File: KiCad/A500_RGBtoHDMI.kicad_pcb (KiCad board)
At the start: 2 copper layers, 80 x 29.5 mm, 19 parts, among them J1 Conn_02x20_Odd_Even, J2 Conn_01x02, U1 Denise_Socket, U2 XC9572XL-VQ64, U3 LM1117-3.3, U4 Denise_MB_PinHeader

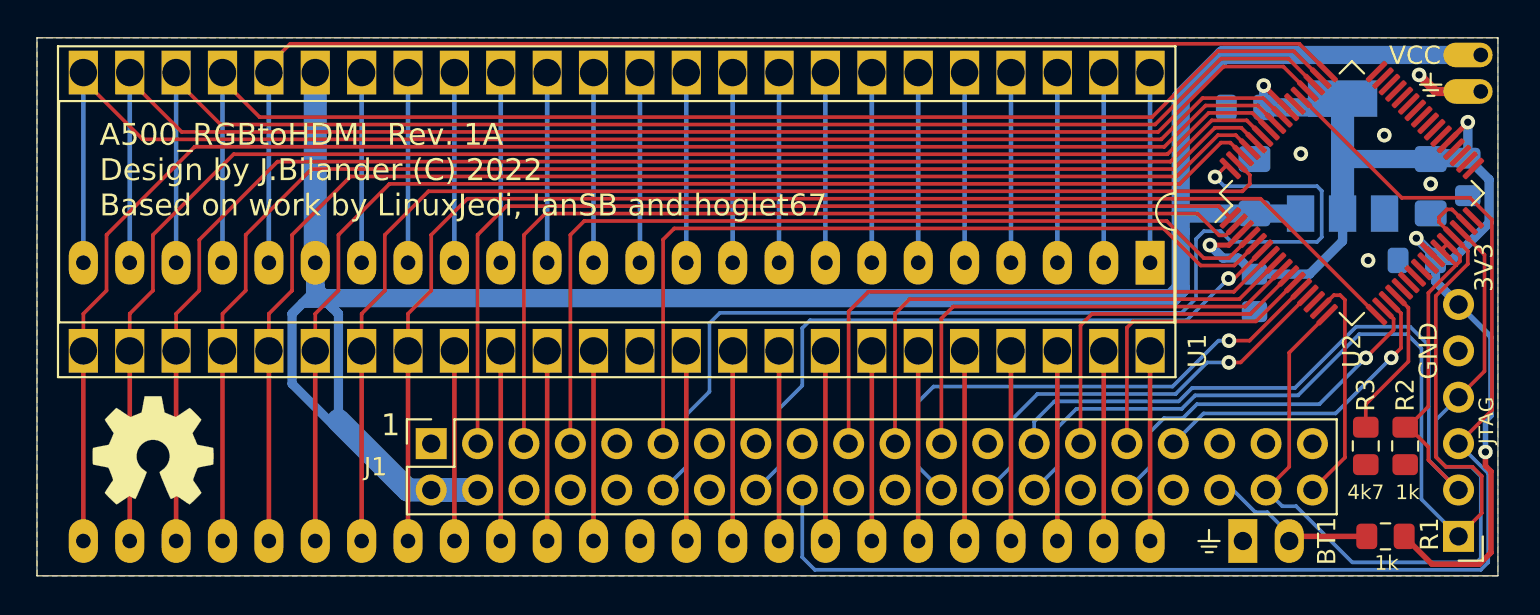
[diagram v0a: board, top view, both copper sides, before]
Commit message: add CSYNC-PinHeader for Rev3 A500-mobos
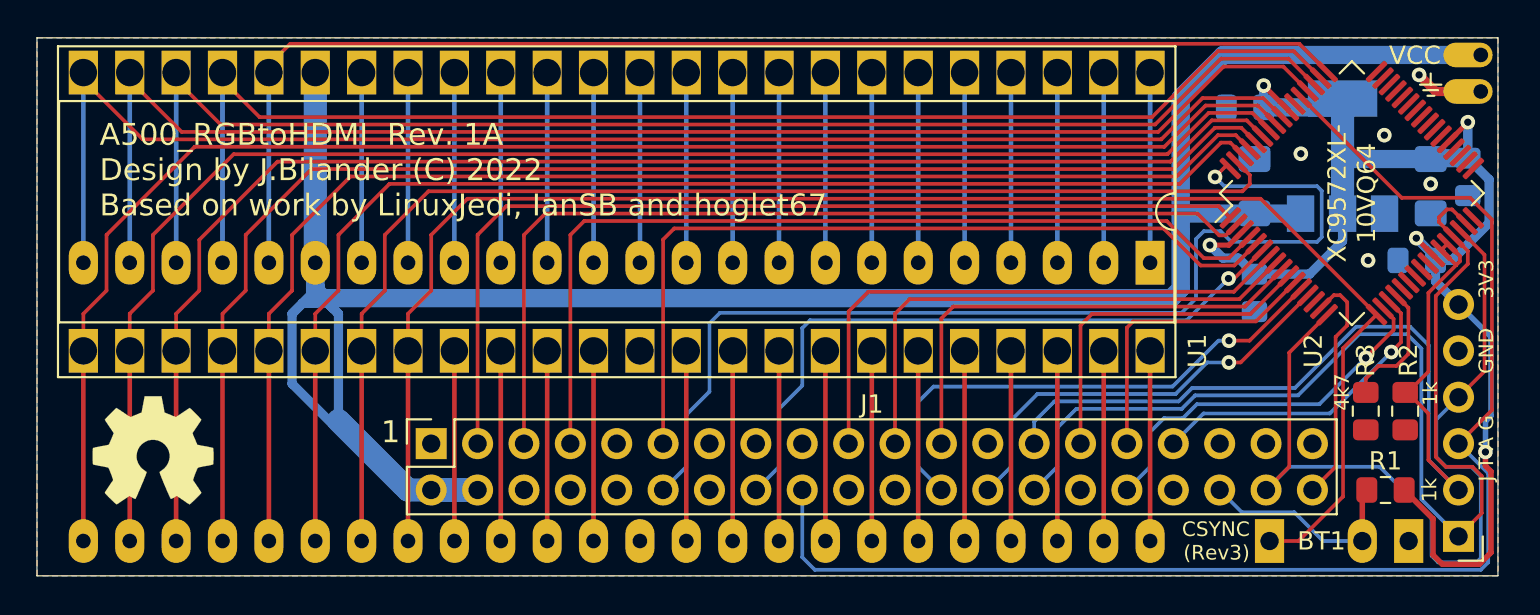
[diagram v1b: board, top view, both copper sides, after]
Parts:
- added J3: Conn_01x01, Connector_PinHeader_2.54mm:PinHeader_1x01_P2.54mm_Horizontal, F.Cu at (194.5, 103.4)
- BT1: moved to F.Cu
- moved BT1 9.08 mm to (202.1, 103.4)
- moved R1 2.54 mm to (200.9, 100.6)
- moved R2 1.91 mm to (201.9, 96.3)
- moved R3 1.91 mm to (199.8, 96.3)
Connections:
- net Net-(U2-Pad48) renamed VSYNC
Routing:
- net CSYNC: track 72.5 -> 88.4 mm
- net TCK_SPCLK: track 45.9 -> 48.1 mm
- net 3V3: track 70.8 -> 73.0 mm
- net Net-(BT1-Pad2): track 9.54 -> 11.7 mm
- net DETECT: track 8.48 -> 7.14 mm
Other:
- net class Default: clearance 0.2032 -> 0.1524
- rule trace_clearance: 0.2032 -> 0.1524
- board text added: "CSYNC"
- board text added: "CSYNC (Rev3)"
- board text added: "J T A G"
- board text added: "XC9572XL- 10VQ64"
- board text removed: "JTAG"

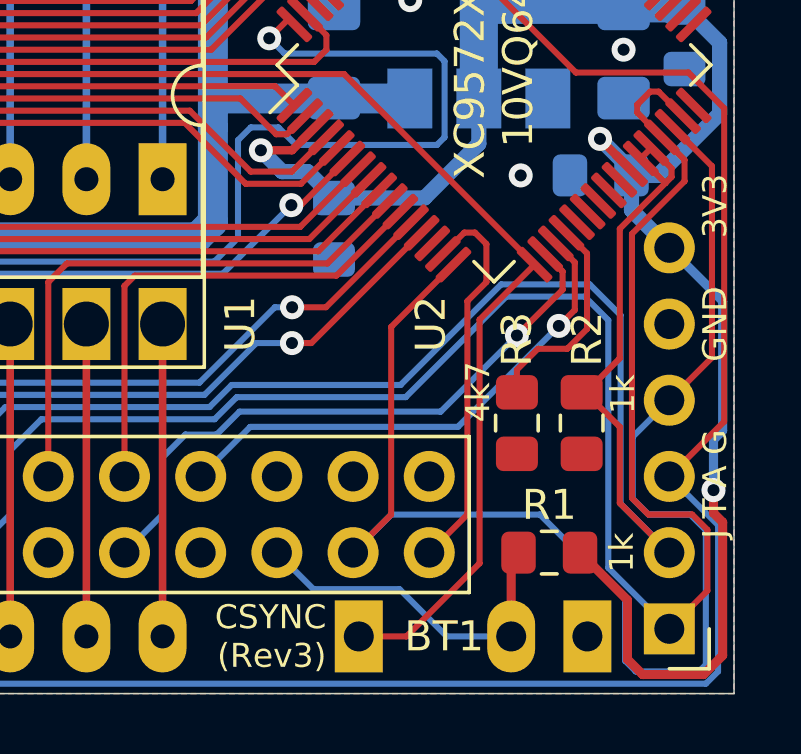
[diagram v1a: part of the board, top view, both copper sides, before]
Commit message: removed pull-up resistor on BT1 (gpio16), not needed
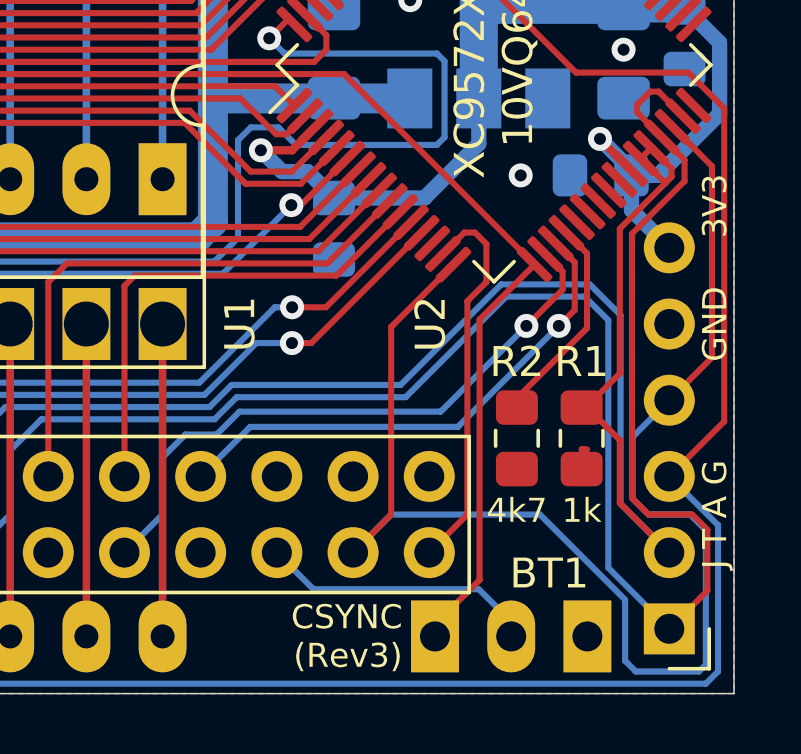
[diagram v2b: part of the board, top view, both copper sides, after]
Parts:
- removed R3: 4.7k, Resistor_SMD:R_0805_2012Metric_Pad1.15x1.40mm_HandSolder
- R2: value 1k -> 4.7k
- moved R1 3.96 mm to (201.9, 96.8), turned to 270 degrees
- moved J3 2.54 mm to (197.0, 103.4)
- moved R2 2.22 mm to (199.8, 96.8)
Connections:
- R1 pad 1: 3V3 -> TDI_SPDATA
- R1 pad 2: Net-(BT1-Pad2) -> GND
- R2 pad 1: TDI_SPDATA -> DETECT
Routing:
- net 3V3: track 73.0 -> 50.5 mm, vias 5 -> 4
- net Net-(BT1-Pad2): track 11.7 -> 9.18 mm
- net CSYNC: track 88.4 -> 86.2 mm
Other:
- board text added: "LM1117 -3.3"

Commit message: some via and silkscreen fixes
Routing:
- net GND: track 4.08 -> 4.07 mm, vias 5 -> 6
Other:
- net class Default: clearance 0.1524 -> 0.2032
- rule trace_clearance: 0.1524 -> 0.2032

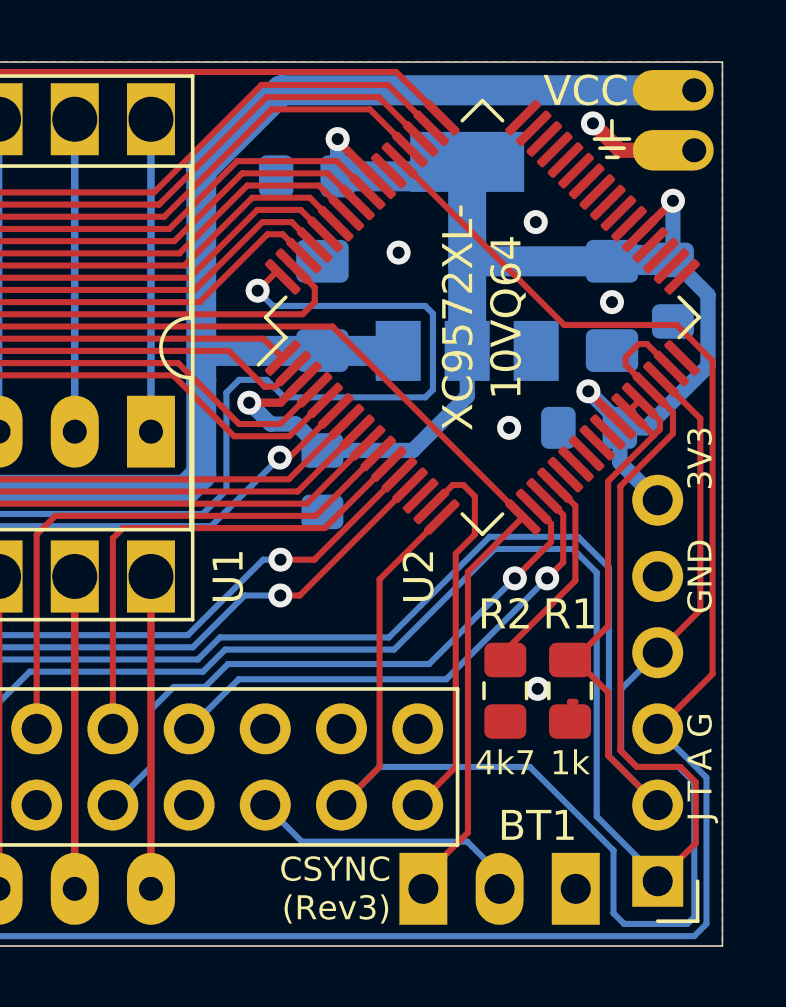
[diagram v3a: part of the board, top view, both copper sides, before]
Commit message: removed hole offset for VCC-header, and some silkscreen fix
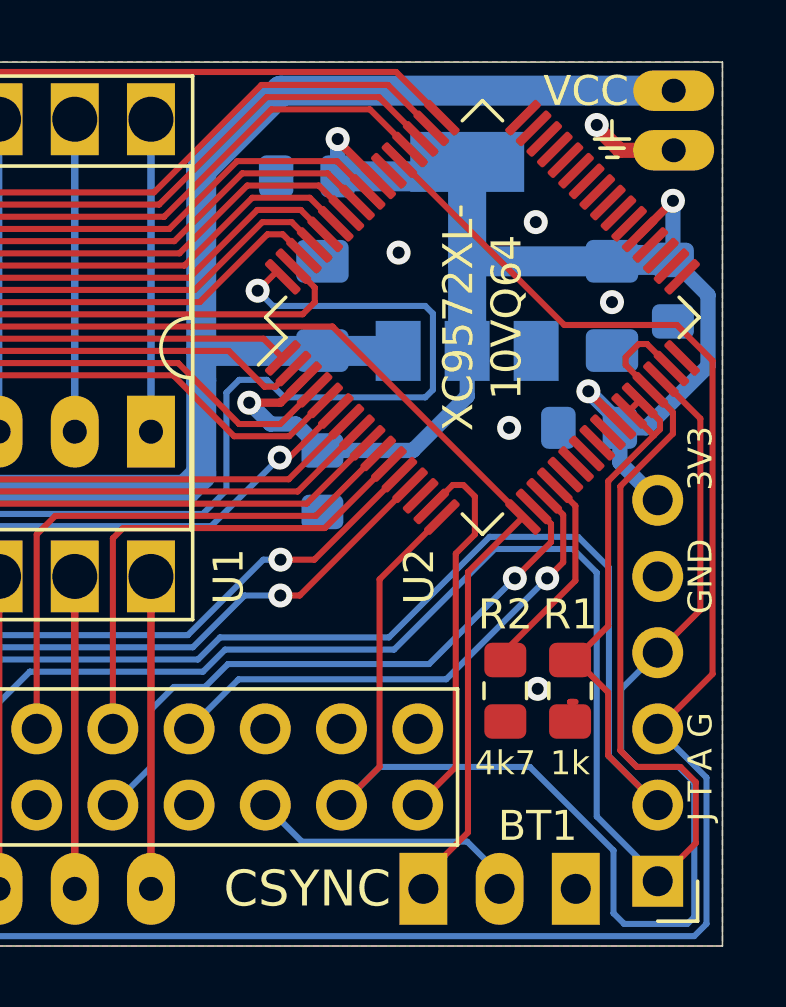
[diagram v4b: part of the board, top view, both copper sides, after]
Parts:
- moved J2 0.69 mm to (205.4, 76.8)
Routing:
- net VCC: track 138.1 -> 137.4 mm
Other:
- board text removed: "CSYNC (Rev3)"
